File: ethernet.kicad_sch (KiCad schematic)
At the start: 34 parts, among them U5 LAN8720A, U6 ARJM11C7-114-BA-EW2, Y1 25MHz

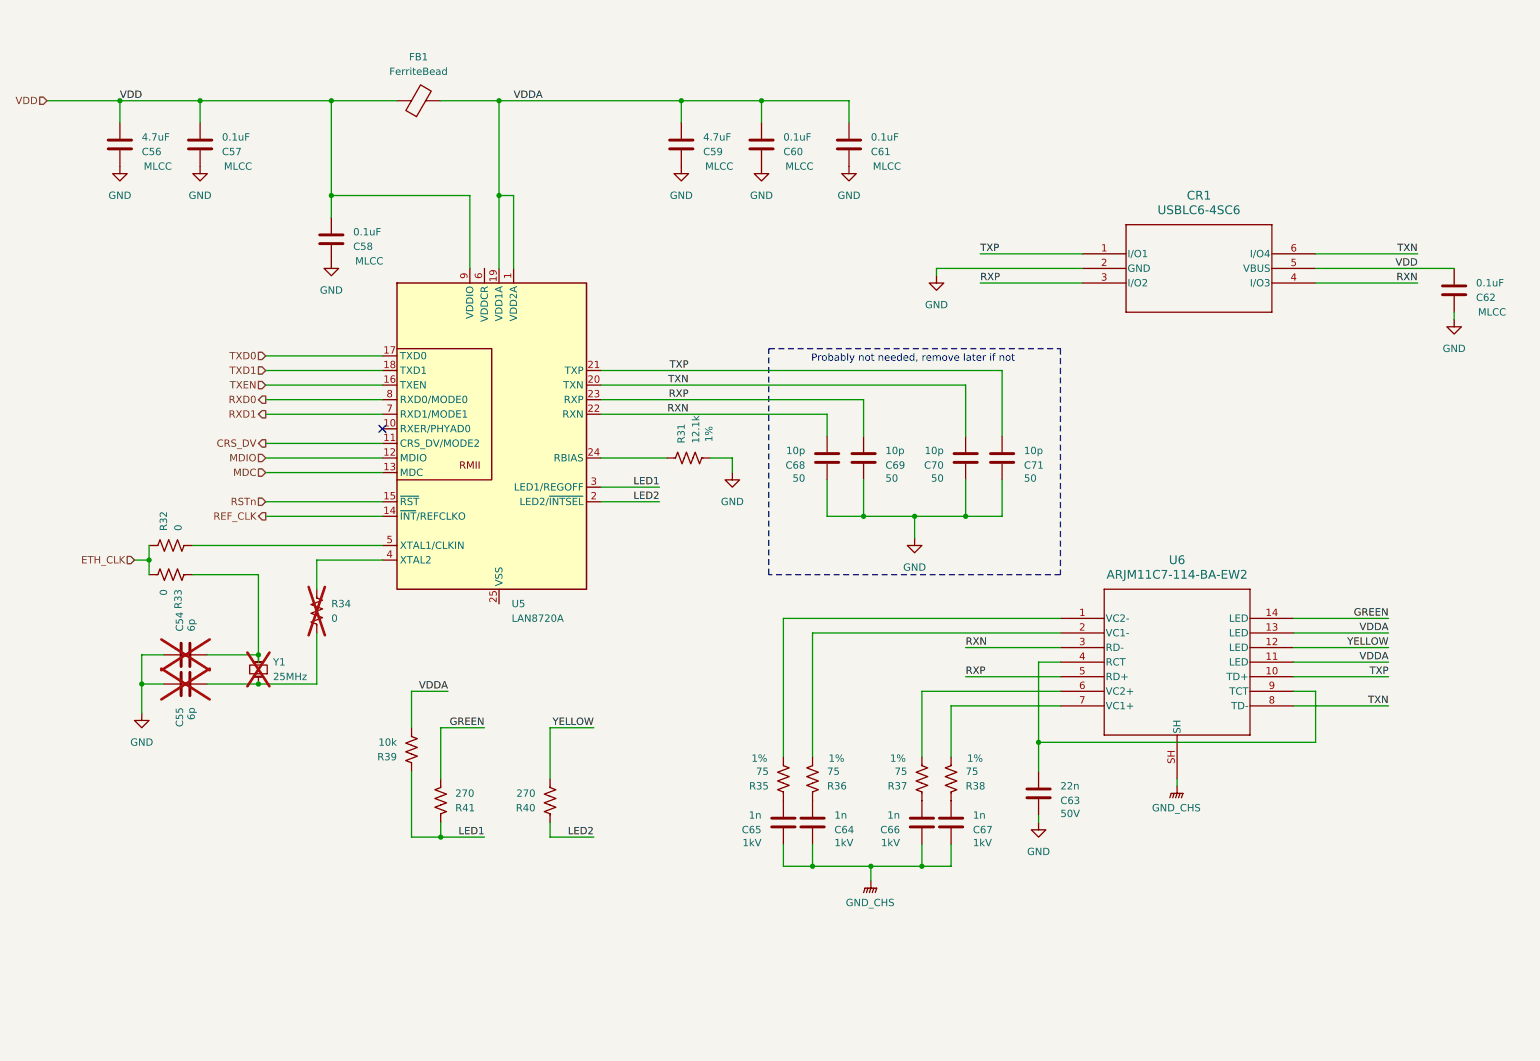
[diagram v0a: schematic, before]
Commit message: Still updating ethernet phy
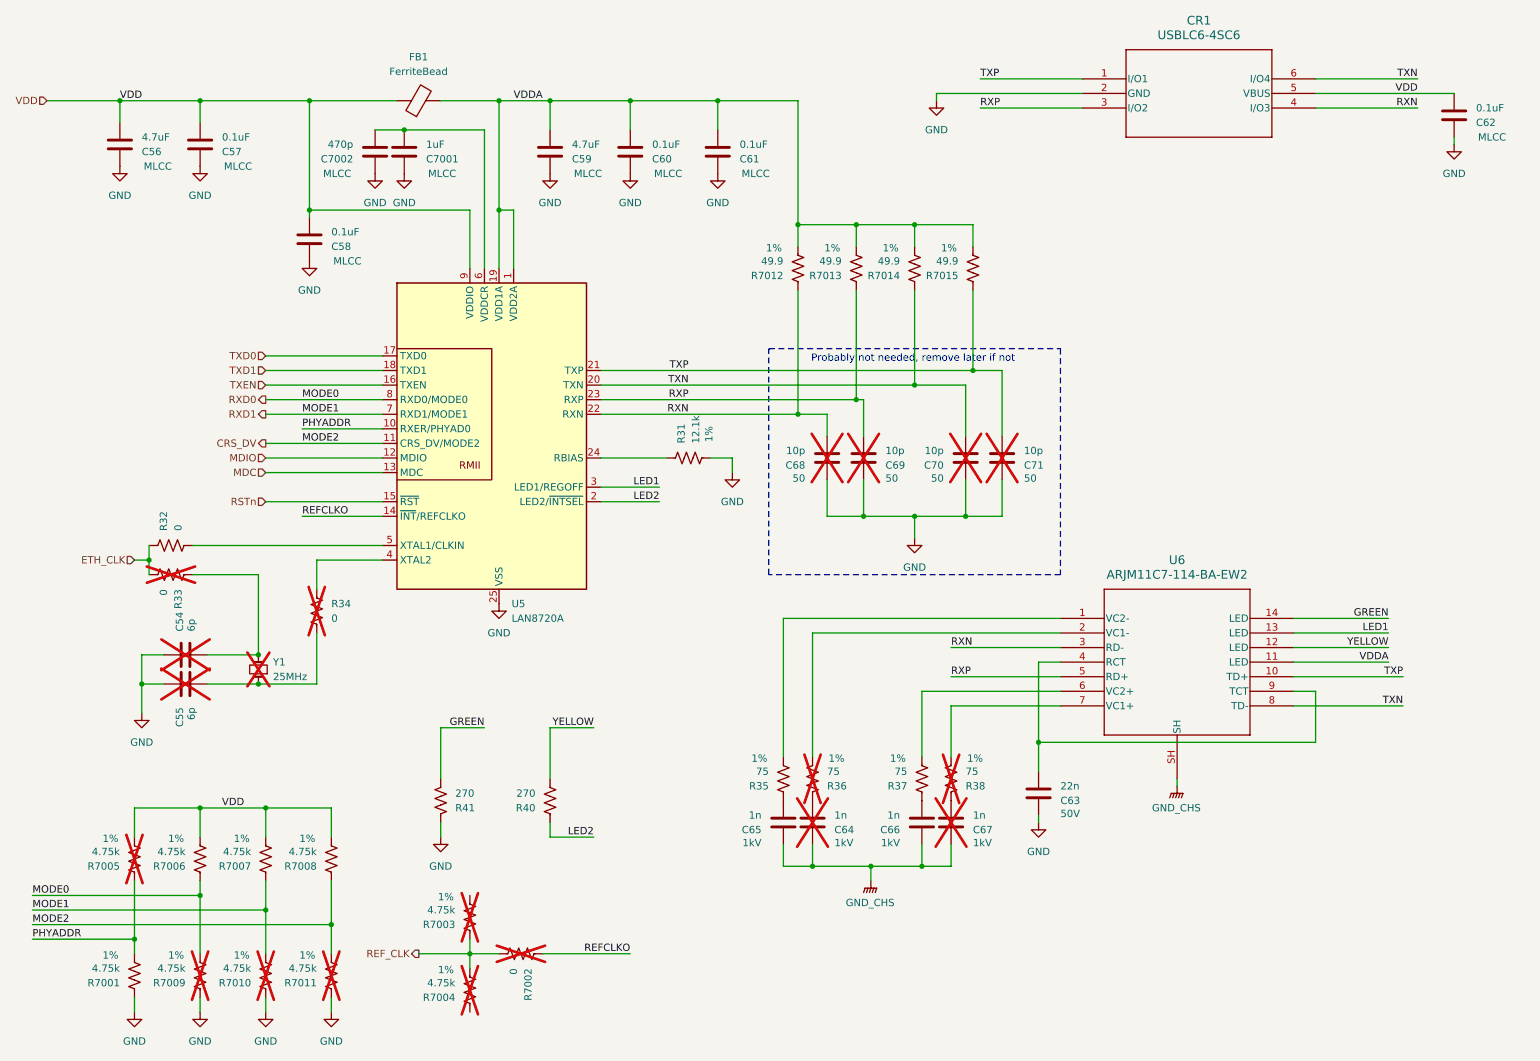
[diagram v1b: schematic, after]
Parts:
- removed R39: 10k, symbol SparkFun-Resistor:R
- added C7001: 1uF, symbol SparkFun-Capacitor:C
- added C7002: 470p, symbol SparkFun-Capacitor:C
- added R7001, R7003, R7004, R7005, R7006, R7007, R7008, R7009, R7010, R7011: 4.75k, symbol SparkFun-Resistor:R
- added R7002: 0, symbol SparkFun-Resistor:R
- added R7012, R7013, R7014, R7015: 49.9, symbol SparkFun-Resistor:R
- C64, C67, C68, C69, C70, C71, R33, R36, R38: now not fitted
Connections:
- net CRS_DV: now also R7008.1, R7011.2
- net GND: now also R41.1, U5.25 (VSS), C7001.2, C7002.2, R7001.1, R7009.1, R7010.1, R7011.1
- net LED1: now also U6.13 (LED); no longer R41.1
- net REF_CLK: now also R7002.2, R7003.1, R7004.2; no longer U5.14 (~{INT}/REFCLKO)
- net RXD0: now also R7006.1, R7009.2
- net RXD1: now also R7007.1, R7010.2
- net RXN: now also R7012.1
- net RXP: now also R7013.1
- net TXN: now also R7014.1
- net TXP: now also R7015.1
- net VDD: now also R7005.2, R7006.2, R7007.2, R7008.2
- net VDDA: now also R7012.2, R7013.2, R7014.2, R7015.2; no longer U6.13 (LED)
- net PHYADDR: now reaches U5.10 (RXER/PHYAD0)
- net PHYADDR: now also R7001.2, R7005.1
- net at U5.6 (VDDCR): now also C7001.1, C7002.1
- new net REFCLKO: R7002.1, U5.14 (~{INT}/REFCLKO)
- no-connect marks 1 -> 0
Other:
- moved on the sheet: C58, C59, C60, C61, C62, CR1

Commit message: Moved connectors to their own sheets
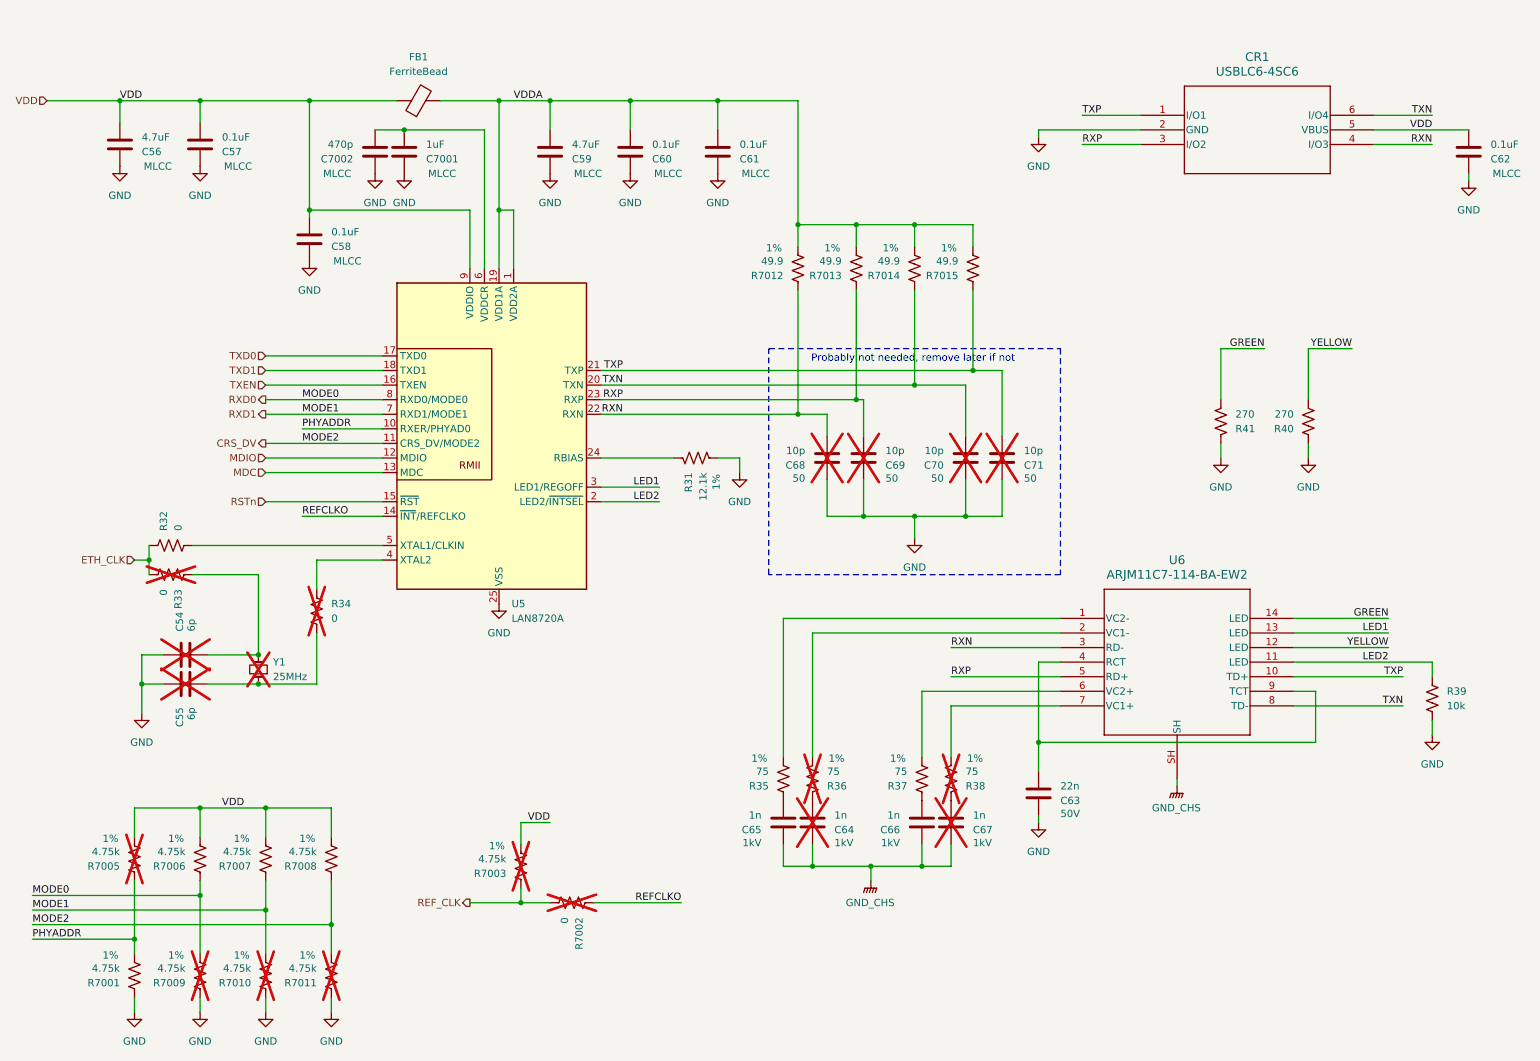
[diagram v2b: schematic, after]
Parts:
- removed R7004: 4.75k, symbol SparkFun-Resistor:R
- added R39: 10k, symbol SparkFun-Resistor:R
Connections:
- net GND: now also R40.1, R39.2
- net LED2: now also U6.11 (LED), R39.1; no longer R40.1
- net VDD: now also R7003.2
- net VDDA: no longer U6.11 (LED)
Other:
- moved on the sheet: C62, CR1, R31, R40, R41, R7002, R7003

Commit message: Adding more decoupling and started on DSI connector
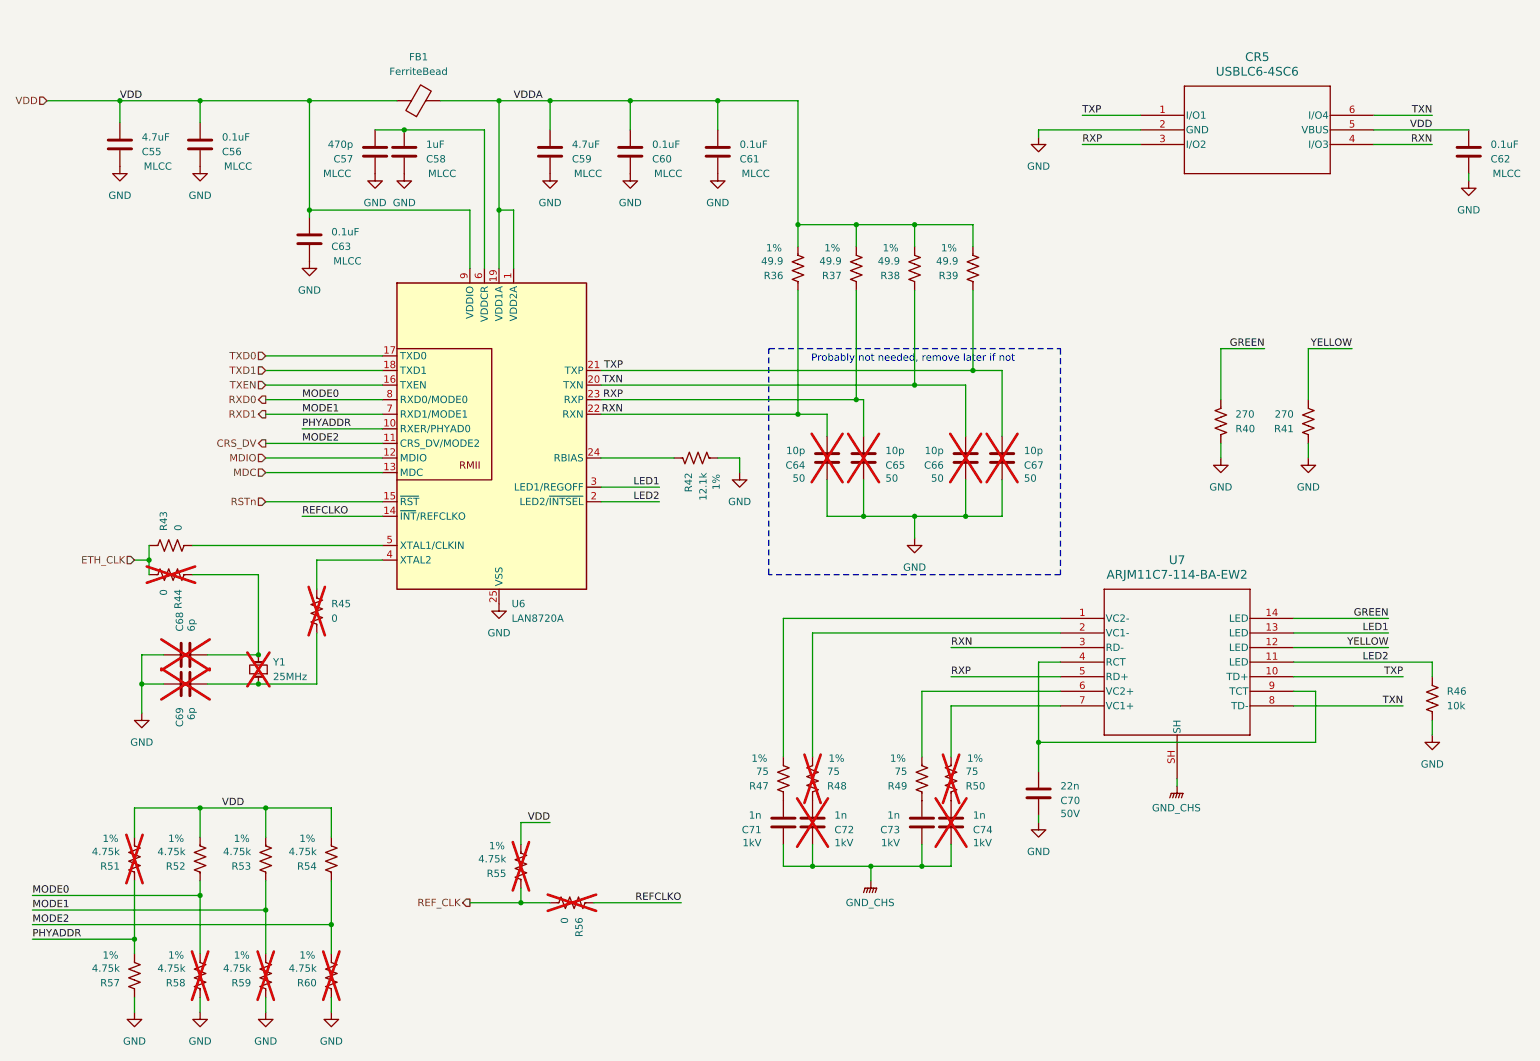
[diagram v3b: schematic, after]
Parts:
- CR5: renamed from CR1; footprint SOT23-6L_STM -> (none)
- FB1: footprint 0805 -> (none)
- U7: renamed from U6; footprint ARJM11C7-114-BA-EW2_ABR -> (none)
- renumbered C56 to C55, C57 to C56, C7002 to C57, C7001 to C58, C58 to C63, C68 to C64, C69 to C65, C70 to C66, C71 to C67, C54 to C68, C55 to C69, C63 to C70, C65 to C71, C64 to C72, C66 to C73, C67 to C74, R7012 to R36, R7013 to R37, R7014 to R38, R7015 to R39, R41 to R40, R40 to R41, R31 to R42, R32 to R43, R33 to R44, R34 to R45, R39 to R46, R35 to R47, R36 to R48, R37 to R49, R38 to R50, R7005 to R51, R7006 to R52, R7007 to R53, R7008 to R54, R7003 to R55, R7002 to R56, R7001 to R57, R7009 to R58, R7010 to R59, R7011 to R60, U5 to U6

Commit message: Selecting footprints
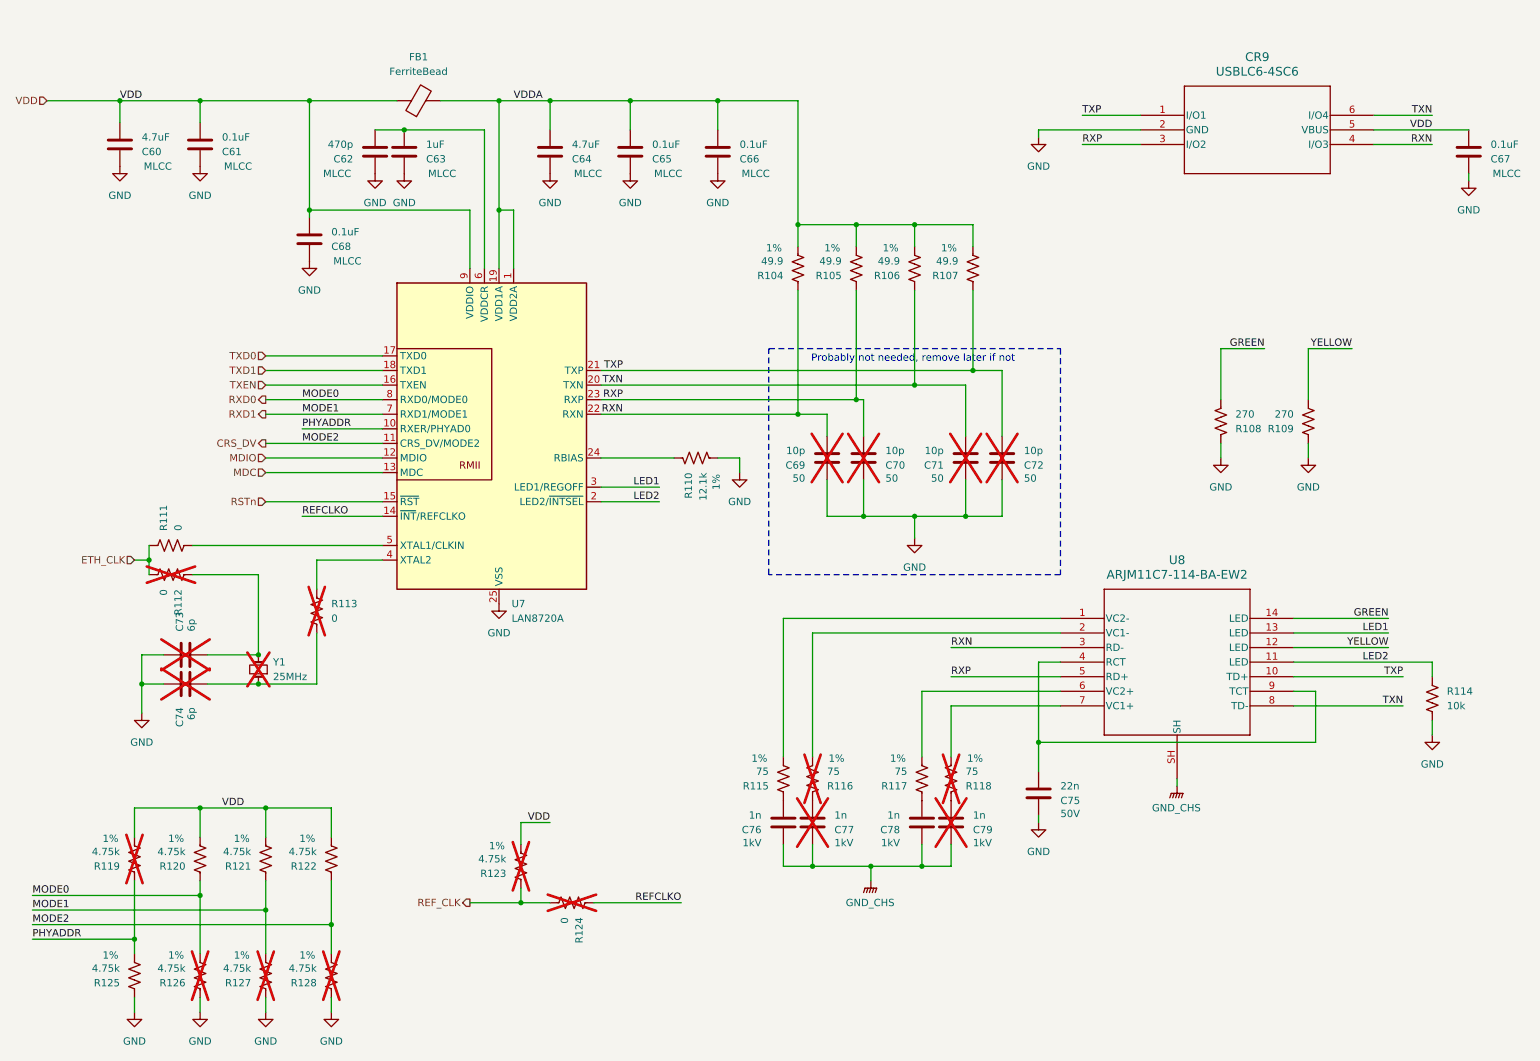
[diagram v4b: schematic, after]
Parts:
- C60: renamed from C55; footprint (none) -> Capacitor_SMD:C_0603_1608Metric
- C61: renamed from C56; footprint (none) -> Capacitor_SMD:C_0402_1005Metric
- C62: renamed from C57; footprint (none) -> Capacitor_SMD:C_0402_1005Metric
- C63: renamed from C58; footprint (none) -> Capacitor_SMD:C_0402_1005Metric
- C64: renamed from C59; footprint (none) -> Capacitor_SMD:C_0603_1608Metric
- C65: renamed from C60; footprint (none) -> Capacitor_SMD:C_0402_1005Metric
- C66: renamed from C61; footprint (none) -> Capacitor_SMD:C_0402_1005Metric
- C67: renamed from C62; footprint (none) -> Capacitor_SMD:C_0402_1005Metric
- C68: renamed from C63; footprint (none) -> Capacitor_SMD:C_0402_1005Metric
- C69: renamed from C64; footprint (none) -> Capacitor_SMD:C_0402_1005Metric
- C70: renamed from C65; footprint (none) -> Capacitor_SMD:C_0402_1005Metric
- C71: renamed from C66; footprint (none) -> Capacitor_SMD:C_0402_1005Metric
- C72: renamed from C67; footprint (none) -> Capacitor_SMD:C_0402_1005Metric
- C73: renamed from C68; footprint (none) -> Capacitor_SMD:C_0402_1005Metric
- C74: renamed from C69; footprint (none) -> Capacitor_SMD:C_0402_1005Metric
- C75: renamed from C70; footprint (none) -> Capacitor_SMD:C_0402_1005Metric
- C76: renamed from C71; footprint (none) -> Capacitor_SMD:C_0402_1005Metric
- C77: renamed from C72; footprint (none) -> Capacitor_SMD:C_0402_1005Metric
- C78: renamed from C73; footprint (none) -> Capacitor_SMD:C_0402_1005Metric
- C79: renamed from C74; footprint (none) -> Capacitor_SMD:C_0402_1005Metric
- R104: renamed from R36; footprint (none) -> Capacitor_SMD:C_0402_1005Metric
- R105: renamed from R37; footprint (none) -> Capacitor_SMD:C_0402_1005Metric
- R106: renamed from R38; footprint (none) -> Capacitor_SMD:C_0402_1005Metric
- R107: renamed from R39; footprint (none) -> Capacitor_SMD:C_0402_1005Metric
- R108: renamed from R40; footprint (none) -> Capacitor_SMD:C_0402_1005Metric
- R109: renamed from R41; footprint (none) -> Capacitor_SMD:C_0402_1005Metric
- R110: renamed from R42; footprint (none) -> Capacitor_SMD:C_0402_1005Metric
- R111: renamed from R43; footprint (none) -> Capacitor_SMD:C_0402_1005Metric
- R112: renamed from R44; footprint (none) -> Capacitor_SMD:C_0402_1005Metric
- R113: renamed from R45; footprint (none) -> Capacitor_SMD:C_0402_1005Metric
- R114: renamed from R46; footprint (none) -> Capacitor_SMD:C_0402_1005Metric
- R115: renamed from R47; footprint (none) -> Capacitor_SMD:C_0402_1005Metric
- R116: renamed from R48; footprint (none) -> Capacitor_SMD:C_0402_1005Metric
- R117: renamed from R49; footprint (none) -> Capacitor_SMD:C_0402_1005Metric
- R118: renamed from R50; footprint (none) -> Capacitor_SMD:C_0402_1005Metric
- R119: renamed from R51; footprint (none) -> Capacitor_SMD:C_0402_1005Metric
- R120: renamed from R52; footprint (none) -> Capacitor_SMD:C_0402_1005Metric
- R121: renamed from R53; footprint (none) -> Capacitor_SMD:C_0402_1005Metric
- R122: renamed from R54; footprint (none) -> Capacitor_SMD:C_0402_1005Metric
- R123: renamed from R55; footprint (none) -> Capacitor_SMD:C_0402_1005Metric
- R124: renamed from R56; footprint (none) -> Capacitor_SMD:C_0402_1005Metric
- R125: renamed from R57; footprint (none) -> Capacitor_SMD:C_0402_1005Metric
- R126: renamed from R58; footprint (none) -> Capacitor_SMD:C_0402_1005Metric
- R127: renamed from R59; footprint (none) -> Capacitor_SMD:C_0402_1005Metric
- R128: renamed from R60; footprint (none) -> Capacitor_SMD:C_0402_1005Metric
- renumbered CR5 to CR9, U6 to U7, U7 to U8
